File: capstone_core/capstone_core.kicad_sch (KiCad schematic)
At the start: 6 parts, among them J1 Conn_01x02_Socket, J2 Conn_01x02_Socket, J3 Conn_01x10_Socket, J4 Conn_01x10_Socket, J6 Conn_01x02_Socket, J7 Conn_02x20_Odd_Even

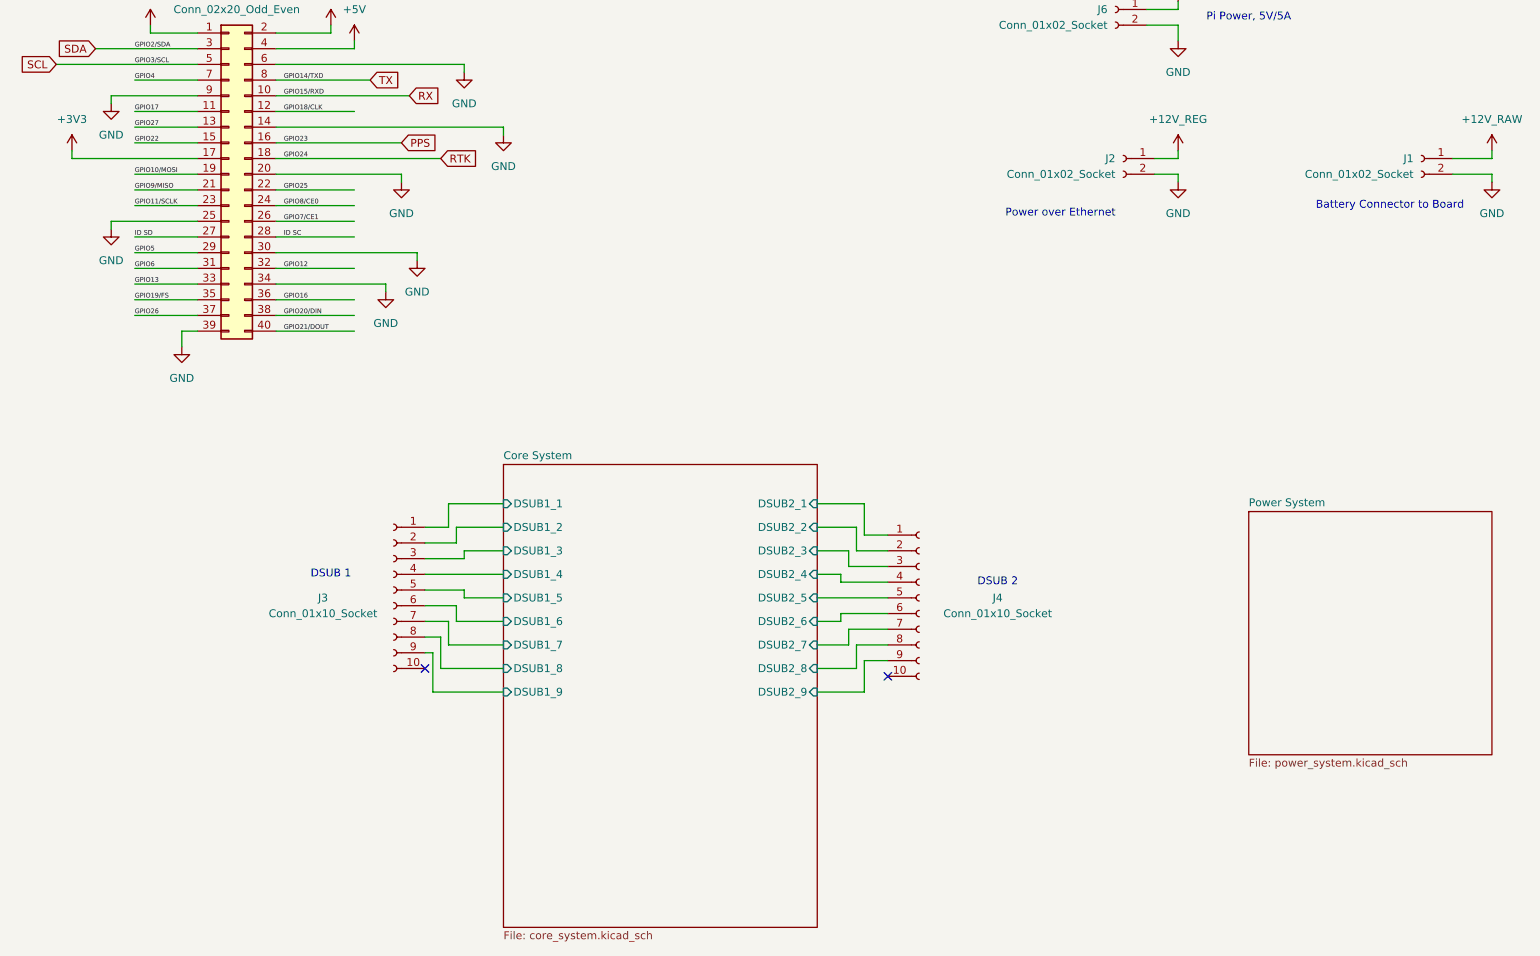
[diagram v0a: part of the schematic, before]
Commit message: moving connectors around
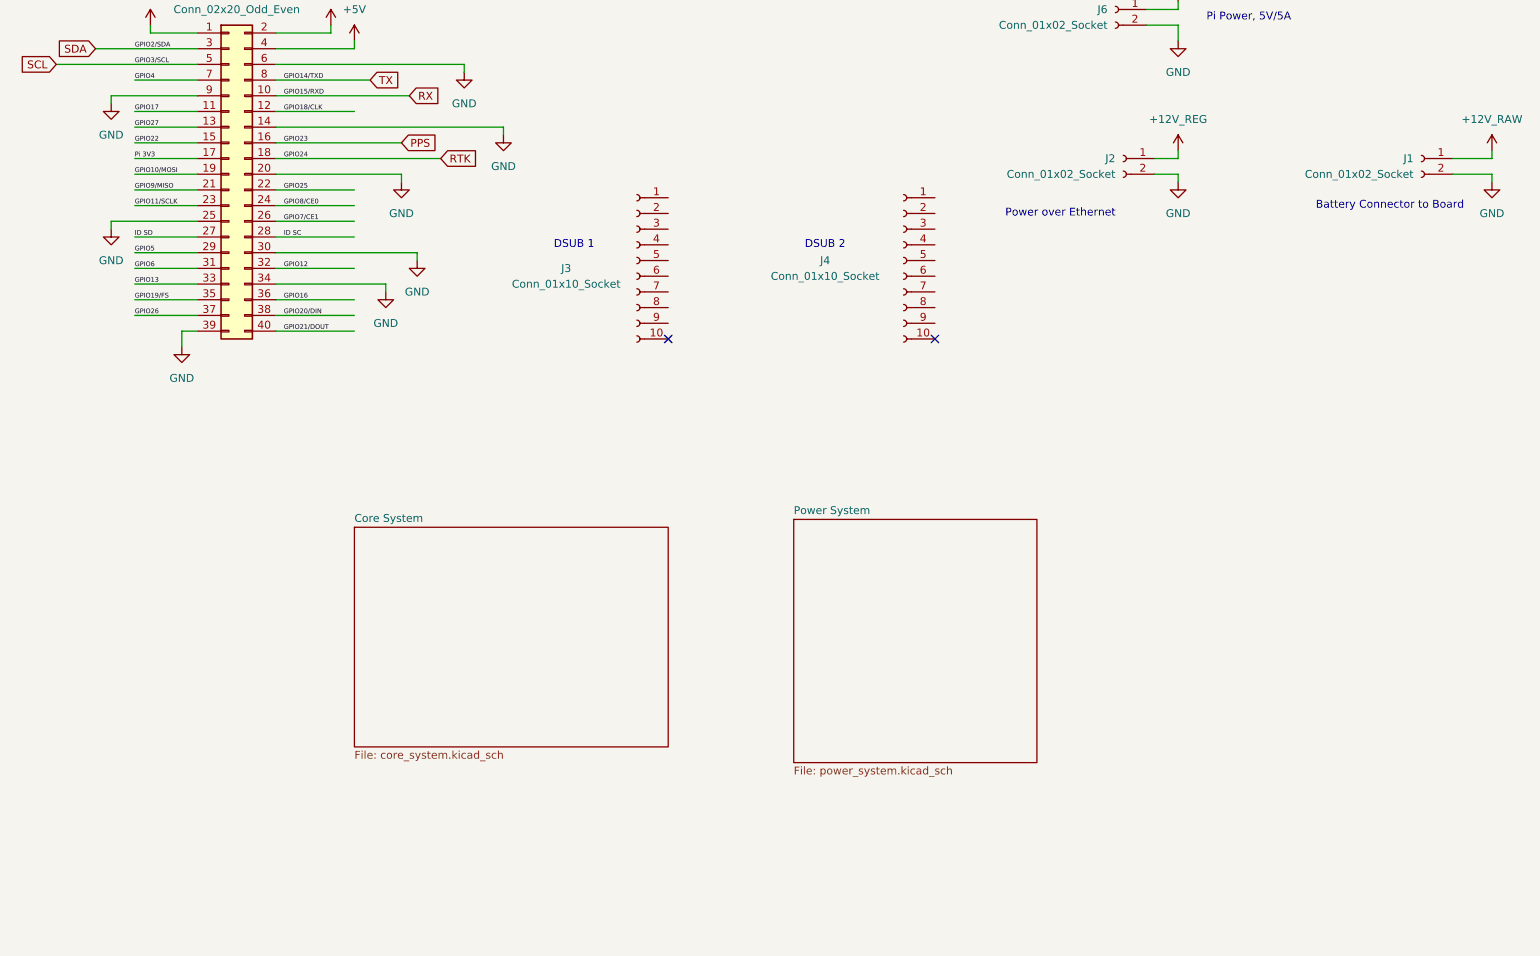
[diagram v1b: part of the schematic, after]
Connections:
- net +3V3: no longer J7.17 (Pin_17)
- net Core System/DSUB1_1: no longer names the net of J3.1 (Pin_1)
- net Core System/DSUB1_2: no longer names the net of J3.2 (Pin_2)
- net Core System/DSUB1_3: no longer names the net of J3.3 (Pin_3)
- net Core System/DSUB1_4: no longer names the net of J3.4 (Pin_4)
- net Core System/DSUB1_5: no longer names the net of J3.5 (Pin_5)
- net Core System/DSUB1_6: no longer names the net of J3.6 (Pin_6)
- net Core System/DSUB1_7: no longer names the net of J3.7 (Pin_7)
- net Core System/DSUB1_8: no longer names the net of J3.8 (Pin_8)
- net Core System/DSUB1_9: no longer names the net of J3.9 (Pin_9)
- net Core System/DSUB2_1: no longer names the net of J4.1 (Pin_1)
- net Core System/DSUB2_2: no longer names the net of J4.2 (Pin_2)
- net Core System/DSUB2_3: no longer names the net of J4.3 (Pin_3)
- net Core System/DSUB2_4: no longer names the net of J4.4 (Pin_4)
- net Core System/DSUB2_5: no longer names the net of J4.5 (Pin_5)
- net Core System/DSUB2_6: no longer names the net of J4.6 (Pin_6)
- net Core System/DSUB2_7: no longer names the net of J4.7 (Pin_7)
- net Core System/DSUB2_8: no longer names the net of J4.8 (Pin_8)
- net Core System/DSUB2_9: no longer names the net of J4.9 (Pin_9)
- new net Pi 3V3: J7.17 (Pin_17)
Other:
- sheet Core System ports: added none; removed DSUB1_1, DSUB1_2, DSUB1_3, DSUB1_4, DSUB1_5, DSUB1_6, DSUB1_7, DSUB1_8, DSUB1_9, DSUB2_1, DSUB2_2, DSUB2_3, DSUB2_4, DSUB2_5, DSUB2_6, DSUB2_7, DSUB2_8, DSUB2_9
- moved on the sheet: J3, J4

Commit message: up to date project
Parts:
- removed J3, J4: Conn_01x10_Socket, Capstone Footprints:2x5_CON10_P100X100-RIBBON_TYC, symbol Connector:Conn_01x10_Socket
- added H1, H2, H3: MountingHole, MountingHole:MountingHole_2.5mm, symbol Mechanical:MountingHole
- added J2, J3: 2x5 CONN DSUB-PCB, Capstone Footprints:2x5_CONN_P100X100-RIBBON_TYC, symbol Capstone Symbols:2x5 CONN DSUB-PCB
- added TP1, TP10, TP11, TP2, TP3, TP4, TP5, TP6, TP7, TP8, TP9: TestPoint, TestPoint:TestPoint_THTPad_D1.0mm_Drill0.5mm, symbol Connector:TestPoint
- added U1: ZED F9P GNSS & RTK Module, Capstone Footprints:ZED-F9P, symbol ZED_F9P:ZED-F9P
- added U2: ~, Capstone Footprints:IMU_Breakout_Module, symbol Capstone Symbols:IMU_Breakout_Module
- renumbered J7 to J1, J1 to J4, J6 to J5, J2 to J6
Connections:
- net +3V3: now also TP6.1, U2.1 (3.3V); no longer J1.1 (Pin_1)
- net GND: now also J2.9, J3.9, TP10.1, TP11.1, TP9.1, U1.1 (GND), U1.19 (GND), U1.25 (GND), U2.3 (GND)
- net GPIO4: now also J2.5
- net GPIO5: now also J2.6
- net PPS: now also U1.7 (PPS)
- net RTK: now also U1.6 (RTK)
- net SCL: now also J2.4, J3.4, U1.3 (SDA), U2.6 (SCL)
- net SDA: now also J2.3, J3.3, U1.4 (SCL), U2.5 (SDA)
- net +12V_RAW renamed +V_BATT
- net +V_BATT: now also TP8.1
- net +12V_REG renamed +12V
- net +12V: now also TP1.1
- removed net +5V: J1.2 (Pin_2), J1.4 (Pin_4), J5.1 (Pin_1)
- net GPIO10/MOSI: no longer names the net of J1.19 (Pin_19)
- net GPIO11/SCLK: no longer names the net of J1.23 (Pin_23)
- net GPIO12: no longer names the net of J1.32 (Pin_32)
- net GPIO13: no longer names the net of J1.33 (Pin_33)
- net GPIO16: no longer names the net of J1.36 (Pin_36)
- net GPIO17: no longer names the net of J1.11 (Pin_11)
- net GPIO18/CLK renamed GPIO18
- net GPIO18: now also J2.7
- net GPIO19/FS renamed GPIO19
- net GPIO19: now also J3.7
- net GPIO20/DIN renamed GPIO20
- net GPIO20: now also J2.8
- net GPIO21/DOUT renamed GPIO21
- net GPIO21: now also J3.8
- net GPIO22: no longer names the net of J1.15 (Pin_15)
- net GPIO25: no longer names the net of J1.22 (Pin_22)
- net GPIO26: no longer names the net of J1.37 (Pin_37)
- net GPIO27: no longer names the net of J1.13 (Pin_13)
- net GPIO6: no longer names the net of J1.31 (Pin_31)
- net GPIO7/CE1: no longer names the net of J1.26 (Pin_26)
- net GPIO8/CE0 renamed GPIO8
- net GPIO8: now also J3.5
- net GPIO9/MISO renamed GPIO9
- net GPIO9: now also J3.6
- net ID SC: no longer names the net of J1.28 (Pin_28)
- net ID SD: no longer names the net of J1.27 (Pin_27)
- net Pi 3V3: no longer names the net of J1.17 (Pin_17)
- net RX renamed RTK_RX
- net RTK_RX: now also U1.21 (TX2)
- net TX renamed RTK_TX
- net RTK_TX: now also U1.22 (RX2)
- new net +1V8: TP7.1, U2.2 (1.8V)
- new net +CORE_5V: TP2.1, U1.18 (5V)
- new net +LBW_3V3: J2.2, J3.2, TP5.1
- new net +LBW_5V: J2.1, J3.1, TP4.1
- new net +PI_5V: J5.1 (Pin_1), TP3.1
- no-connect marks 2 -> 35
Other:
- removed sheet Core System
- removed sheet Power System
- note added: "+12V +CORE_5V +PI_5V +LBW_5V"
- note added: "+1V8"
- note added: "+3V3"
- note added: "+LBW_3V3"
- note added: "+V_BATT"
- note added: "Buck Regulate:"
- note added: "HBW Module Power"
- note added: "IMU Breakout Module"
- note added: "Linear Regulate:"
- note added: "Power Subsystem Voltages:"
- note added: "| V"
- note removed: "Power over Ethernet"
- moved on the sheet: J4, J5, J6
